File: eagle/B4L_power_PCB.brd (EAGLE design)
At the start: 48.2 x 88.6 mm, 39 parts, among them IC1 LM2576S, IC2 TL081CP, Q1 STP40NF03L, U1 TMC2209-LA

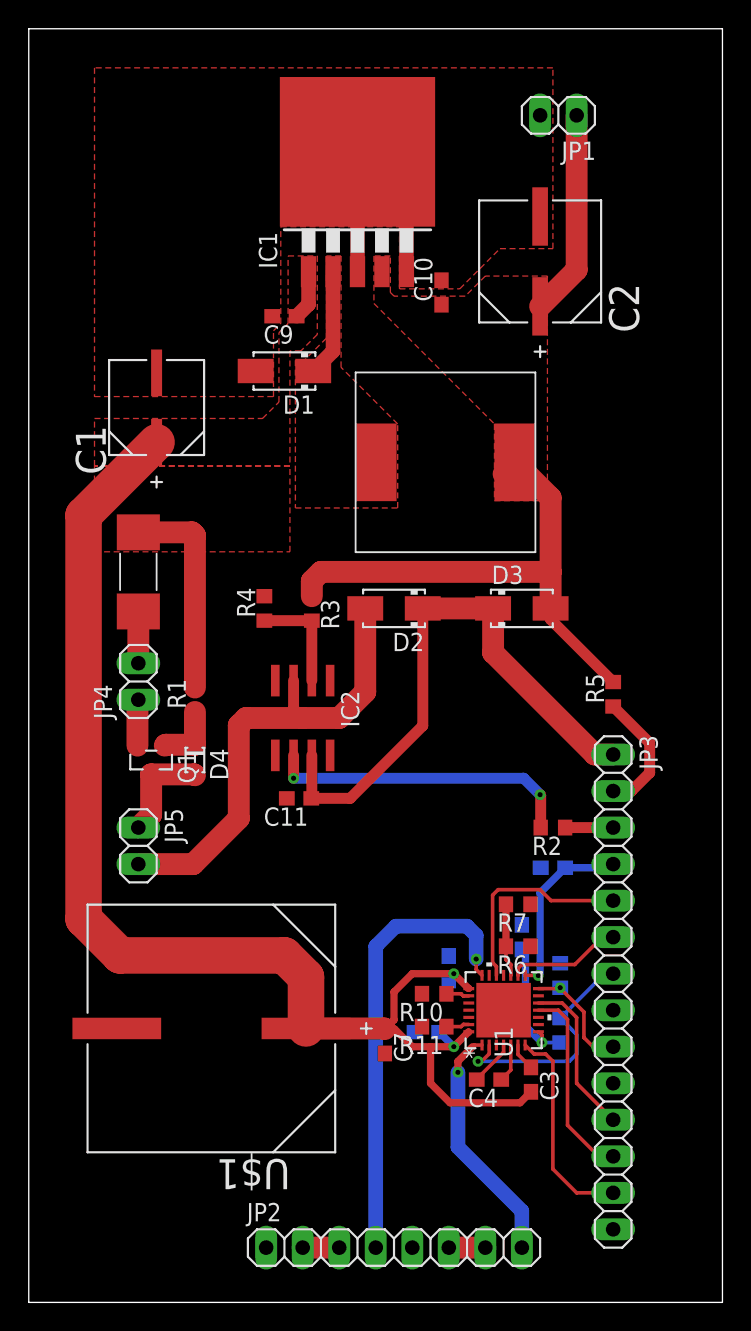
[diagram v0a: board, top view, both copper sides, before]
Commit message: finish initial routing
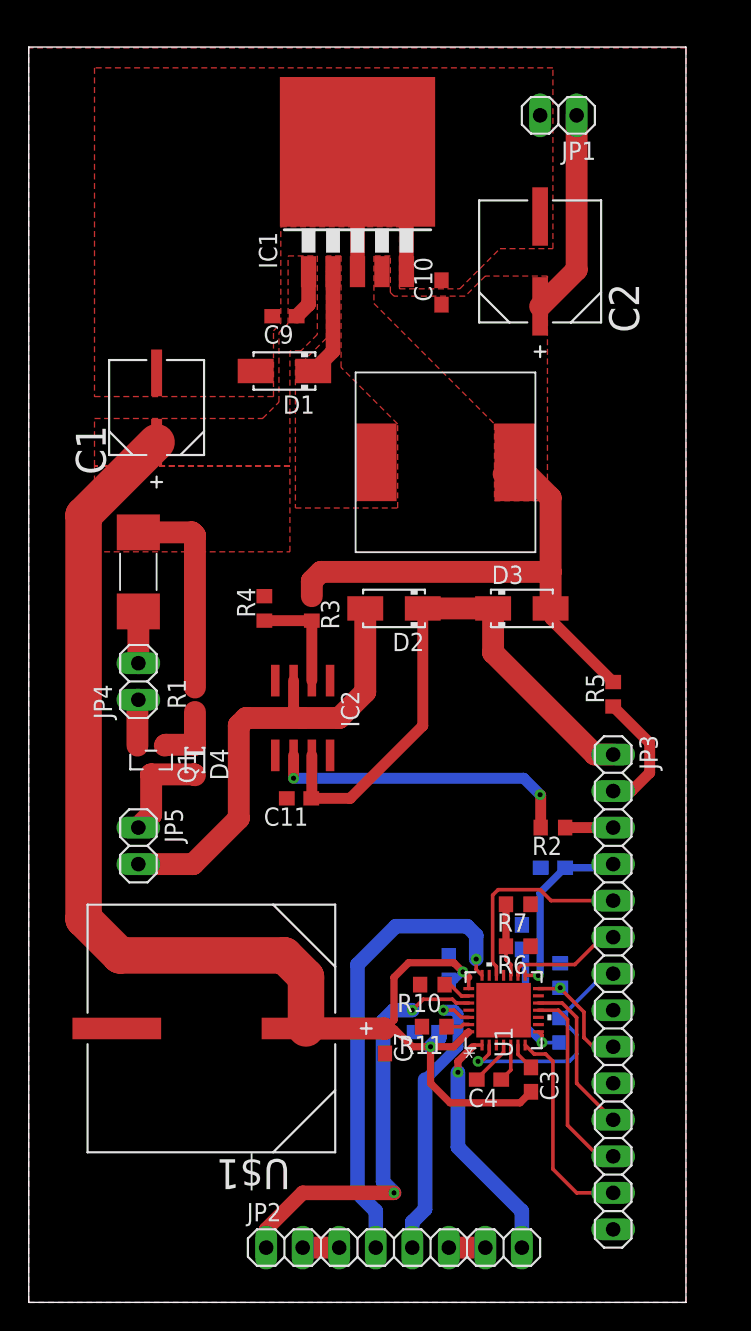
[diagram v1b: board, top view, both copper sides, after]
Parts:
- moved R10 0.65 mm to (28.1, 22.1)
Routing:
- net MOTOR_A: track 0.00 -> 30.2 mm, vias 0 -> 2
- net MOTOR_B: track 0.00 -> 20.7 mm, vias 0 -> 1
- net 24VDC: track 107.7 -> 109.9 mm
- net MOTOR_C: track 31.7 -> 32.8 mm
- added copper zone on layer 16, net GND
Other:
- board size 48.2 x 88.6 mm -> 45.7 x 87.3 mm

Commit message: Update PCB power for 48V supply
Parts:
- removed C11, C5, C6: 100nF, rcl:C0603
- removed C12, C8: 4.7uF, rcl:C0603
- removed C4: 22nF, rcl:C0603
- removed C7: 10uF, rcl:C0603
- removed IC2: TL081CP, custom:SO08
- removed R10, R11: 0.11, rcl:R0603
- removed R3: 56k, rcl:R0603
- removed R4: 100k, rcl:R0603
- removed U$1: EEEFK1H102AM, custom:CAPAE1700X1700N
- removed U1: TMC2209-LA, custom:QFN28_5X5_3X8_EPAD
- added IC3: LM211PSOIC, custom:SO08
- added JP6: (no value), pinhead:1X02
- added LED1: (no value), led:LED3MM
- C1: device Panasonic-EEEFT_EEEH:CAPAE660X800N -> custom:CAPAE1900X2200N
- C3: value 100nF -> 470uF; device rcl:C0603 -> custom:CAPAE1900X1700N
- C9: device rcl:C0603 -> rcl:C1206
- D1, D3: value MBRA340T3G -> B360A-13-F
- D2: value MBRA340T3G -> ES1A+
- F1: value MST 4A 250V -> MCCFB2410TTT/4
- IC1: value LM2576S -> LM2576HVS-12
- JP2: device pinhead:1X08 -> pinhead:1X02
- JP3: device pinhead:1X14 -> pinhead:1X02
- Q1: value STP40NF03L -> SI2356DS-T1-GE3
- R2: value 100k -> 1k
- R6, R8, R9: value 20k -> 100k
- R7: value 20k -> 56k
- moved R2 106.9 mm to (-33.0, -48.3), turned to 0 degrees
- moved JP3 89.9 mm to (-31.8, -31.8), turned to 0 degrees
- moved R9 81.5 mm to (-33.0, -19.1), flipped to the top, turned to 0 degrees
- moved R7 78.9 mm to (-33.0, -14.0), turned to 0 degrees
- moved R8 75.3 mm to (-33.0, -8.89), flipped to the top, turned to 0 degrees
- moved JP2 64.2 mm to (-31.8, -25.4)
- moved C3 48.3 mm to (-12.7, 7.62), turned to 0 degrees
- moved R6 43.5 mm to (1.27, -3.81), turned to 0 degrees
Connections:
- net SUPPLY-24VDC renamed SUPPLY-48VDC
- removed net 24VDC: C1.1, C3.2, C5.1, C6.1, C7.1, C9.1, F1.P$2, IC1.1, R1.2, U$1.1, U1.22, U1.28
- removed net ARD-5VDC: C12.1, JP3.4, U1.15
- removed net MOTOR-DIAG: JP3.12, U1.11
- removed net MOTOR-DIR: JP3.5, U1.19
- removed net MOTOR-EN: JP3.7, R8.1, U1.2
- removed net MOTOR-INDEX: JP3.11, U1.12
- removed net MOTOR-SPRD: JP3.13, U1.7
- removed net MOTOR-STEP: JP3.6, U1.16
- removed net MOTOR-UART: JP3.10, JP3.9, R9.2, U1.14
- removed net MOTOR_A: JP2.1, U1.24
- removed net MOTOR_B: JP2.5, U1.26
- removed net MOTOR_C: JP2.4, U1.21
- removed net MOTOR_D: JP2.8, U1.1
- removed net N$10: R11.1, U1.27
- removed net N$12: JP2.6, JP2.7
- removed net N$5: IC2.6, R2.2
- removed net N$6: R6.2, R7.2, U1.17
- removed net N$7: C4.2, U1.4
- removed net N$8: JP2.2, JP2.3
- removed net N$9: R10.1, U1.23
- removed net TMC-5VDC: C8.1, R6.1, R8.2, U1.8
- removed net TMC-CPI: C4.1, U1.5
- new net 48VDC: C1.1, C3.1, C9.1, F1.P$2, IC1.1, JP6.1, R1.2
- net 12VDC: now also IC3.8, R2.1, R7.1, R9.1; no longer R3.1
- net AUX_PWR_CHK: now also IC3.7, JP3.2, R9.2; no longer JP3.3, R2.1
- net BATT-9VDC: now also IC3.2, R6.1; no longer IC2.3
- net GND: now also C3.2, IC3.1, IC3.4, JP2.2, JP6.2, LED1.K, R6.2, R8.2; no longer C11.2, C12.2, C5.2, C6.2, C7.2, C8.2, IC2.4, JP3.14, R10.2, R11.2, R4.2, R7.1, R9.1, U$1.2, U1.10, U1.13, U1.18, U1.20, U1.29, U1.3, U1.9
- net MAIN_PWR_CHK: now also JP3.1; no longer JP3.2
- net N$3: now also LED1.A, R2.2; no longer IC2.2, R3.2, R4.1
- net N$4: now also IC3.3, R7.2, R8.1; no longer C3.1, U1.6
- net VOUT-12/9VDC: now also JP2.1; no longer C11.1, IC2.7, JP3.1
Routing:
- net 24VDC: track 109.9 -> 0.00 mm, vias 2 -> 0
- net 48VDC: track 0.00 -> 68.1 mm
- net MOTOR_C: track 32.8 -> 0.00 mm, vias 1 -> 0
- net MOTOR_A: track 30.2 -> 0.00 mm, vias 2 -> 0
- net N$5: track 21.5 -> 0.00 mm, vias 2 -> 0
- net MOTOR_B: track 20.7 -> 0.00 mm, vias 1 -> 0
- net MOTOR_D: track 16.9 -> 0.00 mm, vias 1 -> 0
- net MOTOR-EN: track 16.6 -> 0.00 mm, vias 1 -> 0
- net MOTOR-SPRD: track 14.8 -> 0.00 mm
- net MOTOR-DIR: track 14.5 -> 0.00 mm
- net MOTOR-DIAG: track 13.7 -> 0.00 mm
- net ARD-5VDC: track 12.6 -> 0.00 mm, vias 1 -> 0
- net MOTOR-INDEX: track 11.2 -> 0.00 mm
- net TMC-5VDC: track 9.17 -> 0.00 mm, vias 1 -> 0
- net MOTOR-UART: track 8.02 -> 0.00 mm, vias 1 -> 0
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- added copper zone on layer 1, net 48VDC
- removed copper zone on layer 1, net 24VDC
